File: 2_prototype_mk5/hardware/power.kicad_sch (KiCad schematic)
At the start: 6 parts

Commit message: Successful MKV software test (after minor modification)
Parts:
- R5: value 33R -> 47R; LCSC_Part_Number (none) -> C3013388; Manufacturer_Part_Number SR1206FR-7W33RL -> SR2512FK-7W47RL
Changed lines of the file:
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@@
 			)
 		)
-		(property "Value" "33R"
+		(property "Value" "47R"
 			(at 171.45 68.5799 0)
 			(show_name no)
@@
 			)
 		)
-		(property "Description" "Resistor 33 OHM 1% 1/2W 1206 ANTI-SURGE"
+		(property "Description" "Yageo, 47Ω, ±1%, 2W, anti-surge, 2512"
 			(at 168.91 67.31 0)
 			(hide yes)
@@
 			)
 		)
-		(property "Manufacturer_Part_Number" "SR1206FR-7W33RL"
+		(property "Manufacturer_Part_Number" "SR2512FK-7W47RL"
 			(at 168.91 67.31 0)
 			(hide yes)
@@
 			)
 		)
-		(property "LCSC_Part_Number" ""
+		(property "LCSC_Part_Number" "C3013388"
 			(at 168.91 67.31 0)
 			(hide yes)

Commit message: MKV revision 1
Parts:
- added H14: Conn_01x02, Connector_PinHeader_2.54mm:PinHeader_1x02_P2.54mm_Vertical, symbol Connector_Generic:Conn_01x02
- D1: LCSC Part Number (none) -> C2480; LCSC_Part_Number C2480 -> (none)
- D2: LCSC Part Number (none) -> C2479; LCSC_Part_Number C2479 -> (none)
- R3: LCSC Part Number (none) -> C21190; LCSC_Part_Number C21190 -> (none)
- R4: LCSC Part Number (none) -> C4184; LCSC_Part_Number C4184 -> (none)
- R5: value 47R -> 22R; LCSC Part Number (none) -> C5204054; LCSC_Part_Number C3013388 -> (none); Manufacturer_Part_Number SR2512FK-7W47RL -> SR2512FK-7W22RL
- Super_Cap1: now not fitted; now left out of the parts list
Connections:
- net +5V: now also H14.1 (Pin_1)
- net GND: now also H14.2 (Pin_2)
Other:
- note added: "Auxiliary power input"

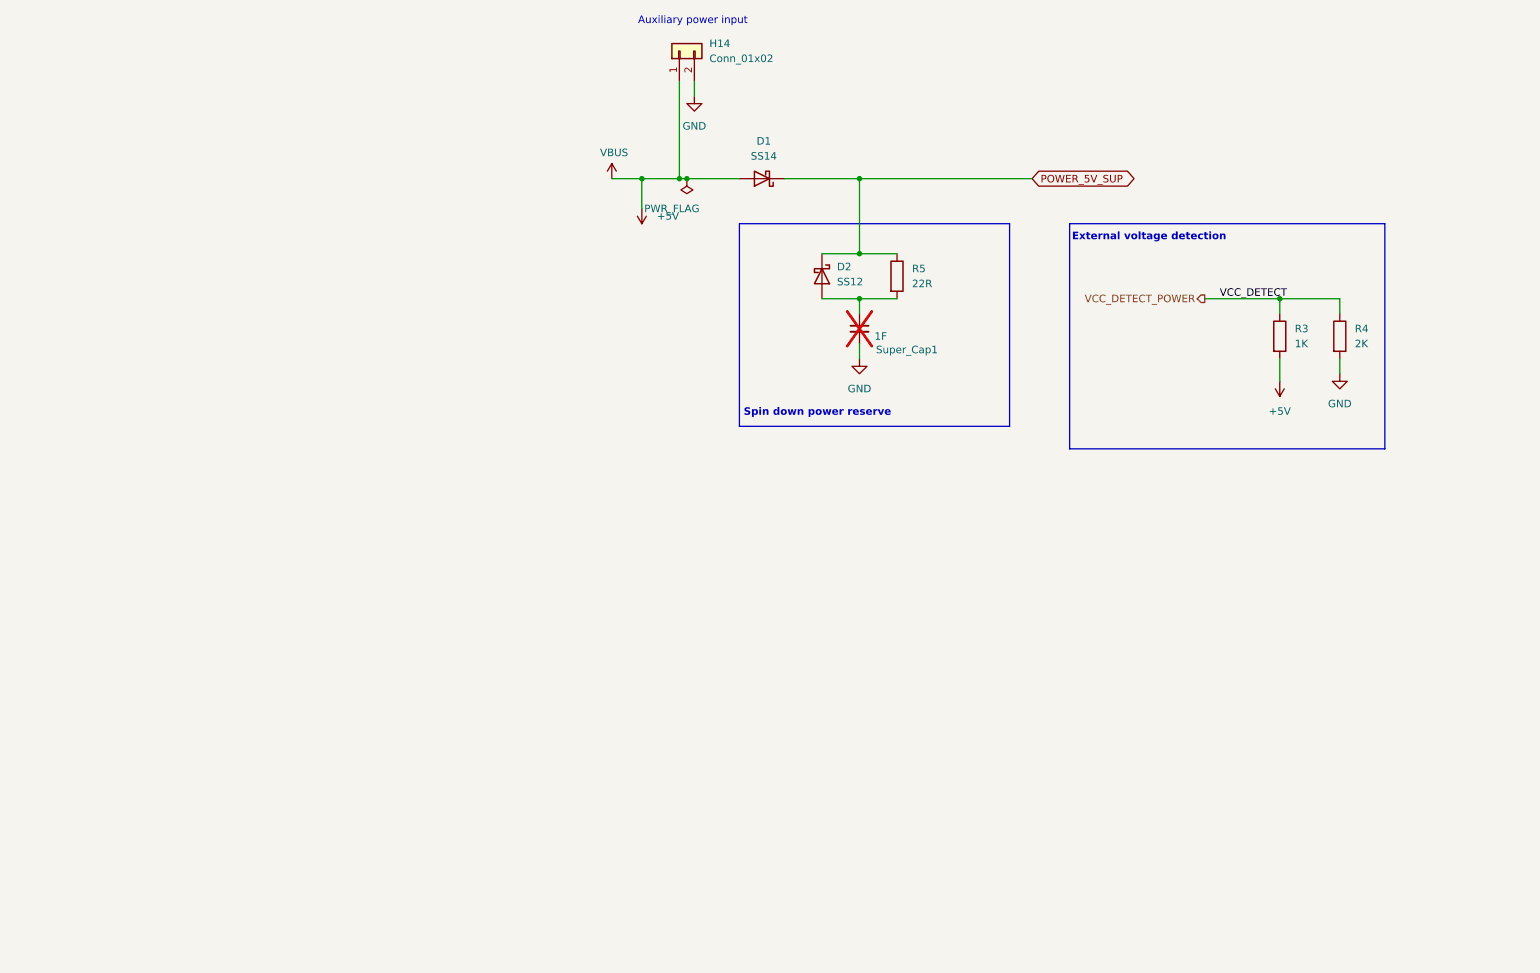
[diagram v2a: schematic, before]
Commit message: Add buck boost to 5V and reset line stability
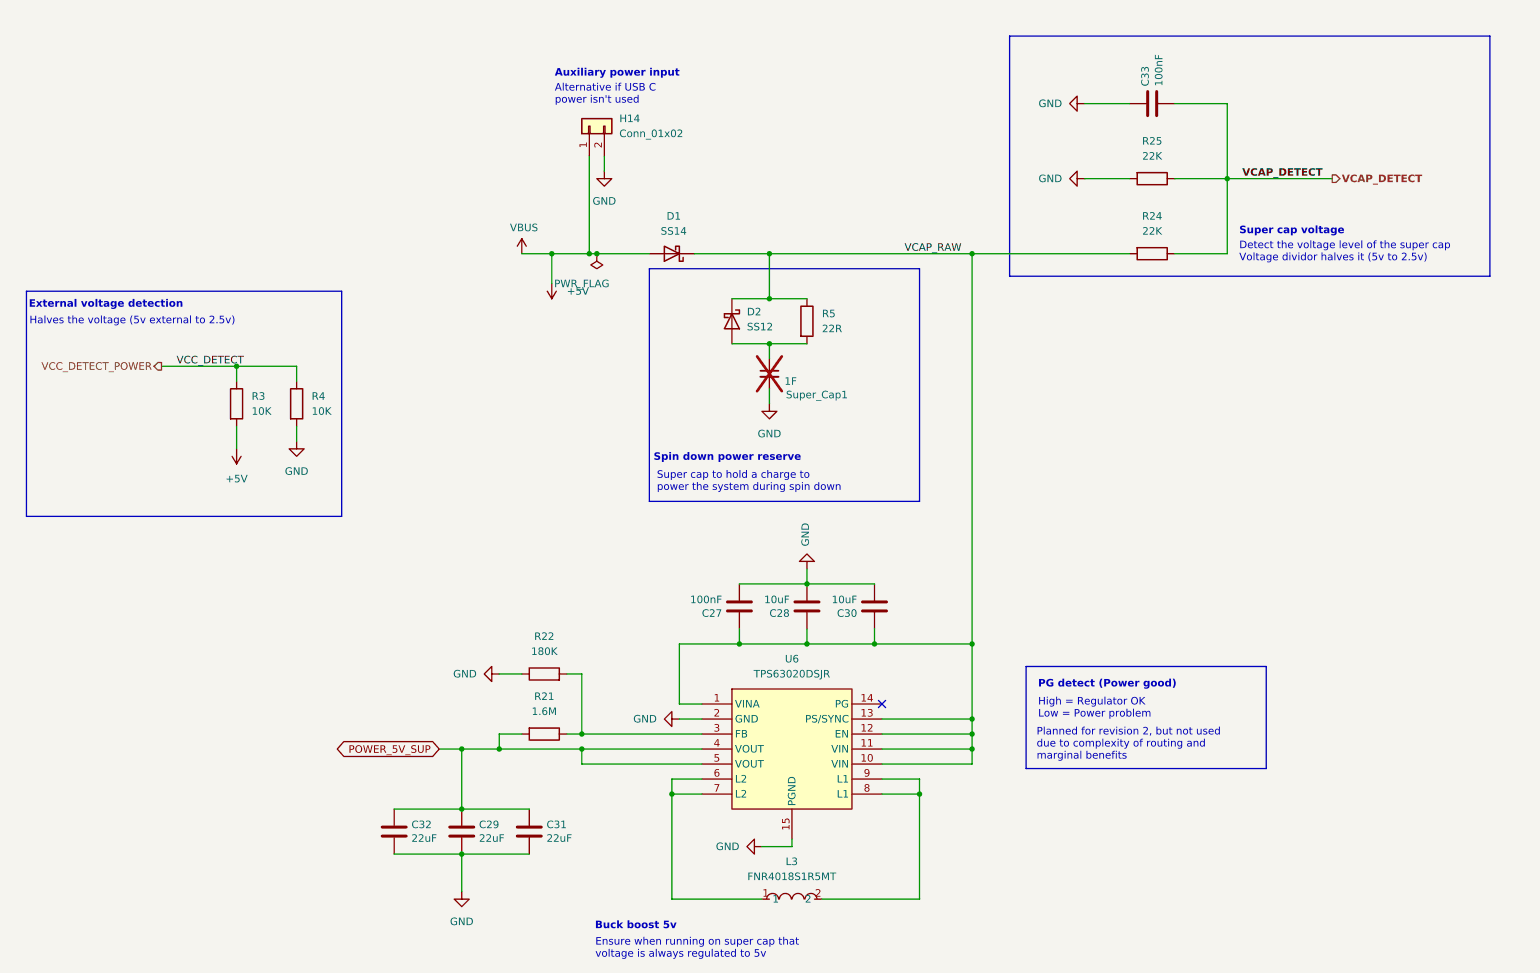
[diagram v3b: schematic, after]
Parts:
- added C27, C33: 100nF, Capacitor_SMD:C_0402_1005Metric, symbol Device:C
- added C28, C30: 10uF, Capacitor_SMD:C_0805_2012Metric, symbol Device:C
- added C29, C31, C32: 22uF, Capacitor_SMD:C_0805_2012Metric, symbol Device:C
- added L3: FNR4018S1R5MT, easyeda2kicad:IND-SMD_L4.0-W4.0_FNR40XXS, symbol easyeda2kicad:FNR4018S1R5MT
- added R21: 1.6M, Resistor_SMD:R_0402_1005Metric, symbol Device:R
- added R22: 180K, Resistor_SMD:R_0402_1005Metric, symbol Device:R
- added R24, R25: 22K, Resistor_SMD:R_0603_1608Metric, symbol Device:R
- added U6: TPS63020DSJR, easyeda2kicad:VSON-14_L4.0-W3.0-P0.50-BL-EP_TI_DSJ, symbol easyeda2kicad:TPS63020DSJR
- R3: value 1K -> 10K
- R4: value 2K -> 10K
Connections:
- net GND: now also C27.2, C28.2, C29.2, C30.2, C31.2, C32.2, C33.1, R22.1, R25.2, U6.15 (PGND), U6.2 (GND)
- net POWER_5V_SUP: now also C29.1, C31.1, C32.1, R21.2, U6.4 (VOUT), U6.5 (VOUT); no longer D1.1 (K), D2.1 (K), R5.1
- new net: L3.1, U6.6 (L2), U6.7 (L2)
- new net: L3.2, U6.8 (L1), U6.9 (L1)
- new net: R21.1, R22.2, U6.3 (FB)
- new net VCAP_DETECT: C33.2, R24.1, R25.1
- new net VCAP_RAW: C27.1, C28.1, C30.1, D1.1 (K), D2.1 (K), R24.2, R5.1, U6.1 (VINA), U6.10 (VIN), U6.11 (VIN), U6.12 (EN), U6.13 (PS/SYNC)
- no-connect marks 0 -> 1
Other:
- note added: "Alternative if USB C power isn't used"
- note added: "Buck boost 5v"
- note added: "Detect the voltage level of the super cap Voltage dividor halves it (5v to 2.5v)"
- note added: "Ensure when running on super cap that voltage is always regulated to 5v"
- note added: "Halves the voltage (5v external to 2.5v)"
- note added: "High = Regulator OK Low = Power problem"
- note added: "PG detect (Power good)"
- note added: "Planned for revision 2, but not used due to complexity of routing and marginal benefits"
- note added: "Super cap to hold a charge to power the system during spin down"
- note added: "Super cap voltage"
- moved on the sheet: D1, D2, H14, R3, R4, R5, Super_Cap1

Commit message: Cost reductions for JCLPCB
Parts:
- removed R21: 1.6M, Resistor_SMD:R_0402_1005Metric, symbol Device:R
- added R30, R31: 100K, Resistor_SMD:R_0402_1005Metric, symbol Device:R
- C29, C31, C32: LCSC Part Number C15850 -> C45783
- D2: value SS12 -> SS14; LCSC Part Number C2479 -> C2480
- H14: now not fitted; now left out of the parts list
- R22: value 180K -> 22K; LCSC Part Number C25905 -> C25768
- R24, R25: LCSC Part Number C21190 -> C31850
- R3: LCSC Part Number C21190 -> C25804
- R4: LCSC Part Number C4184 -> C25804
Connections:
- net POWER_5V_SUP: now also R31.1
- net at R22.2, U6.3 (FB): now also R30.2
- new net: R30.1, R31.2
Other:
- note added: "Changed from original R22 180K / R21 1.6M in spec sheet to LCSC basic parts to save money, but keep same voltage divider"
